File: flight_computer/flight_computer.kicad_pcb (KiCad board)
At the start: 4 copper layers, 89 parts, among them J1 Conn_02x05_Odd_Even, J2 MEM2061-01-188-00-A_REVA, J3 Conn_01x02, J4 Conn_01x07, J5 3817564, Q1 Q_NPN_BEC, Q2 Q_NMOS_GSD, SW1 SW_Push, SW2 SW_Push, U1 STM8S007C8T6TR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

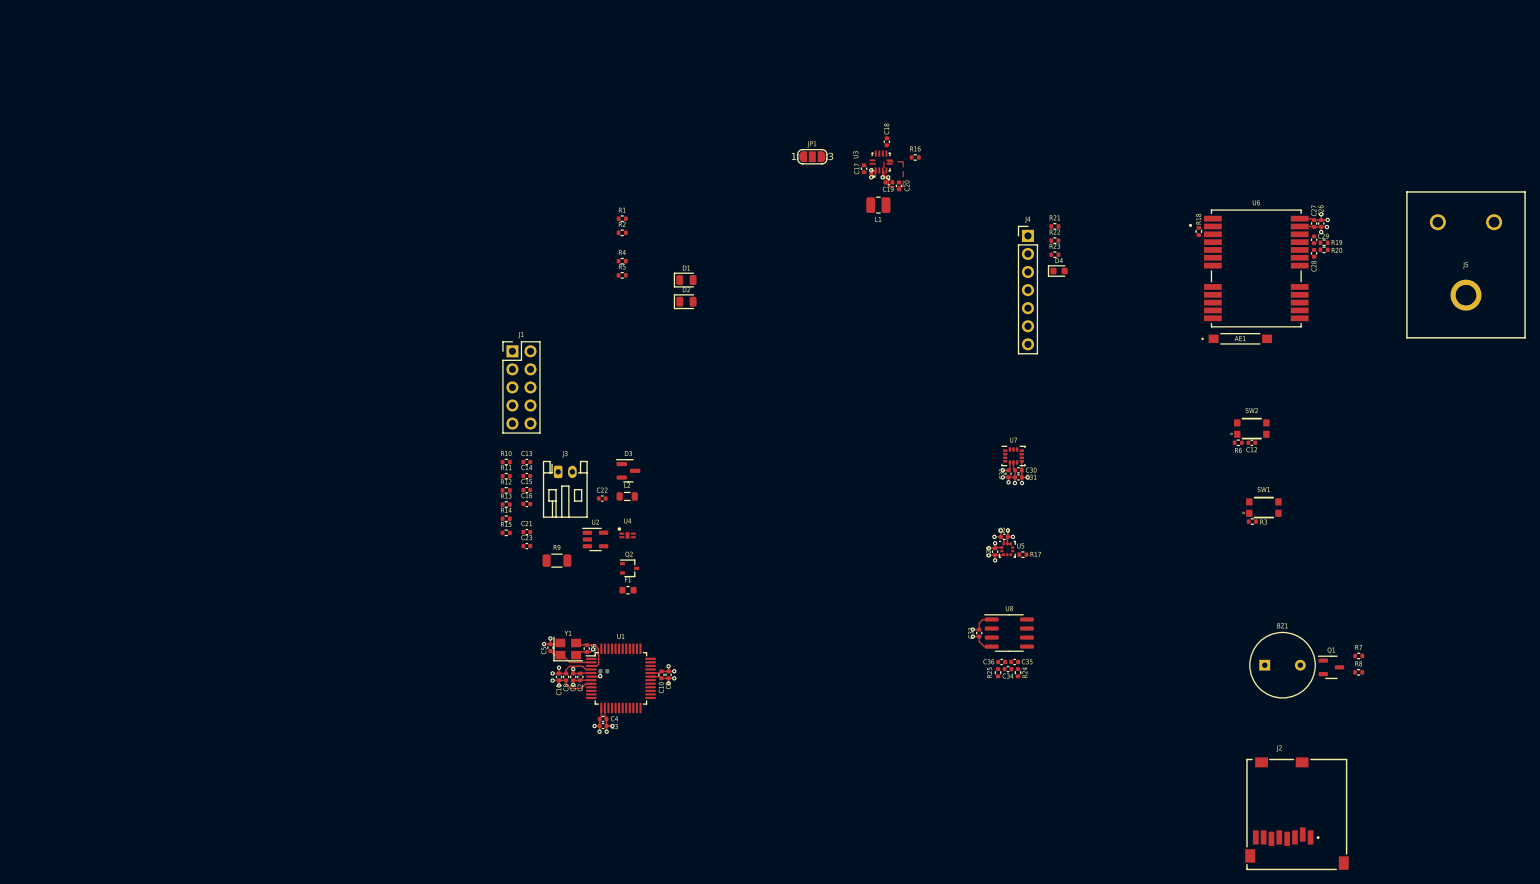
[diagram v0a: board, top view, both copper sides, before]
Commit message: finsihed grouping the layout
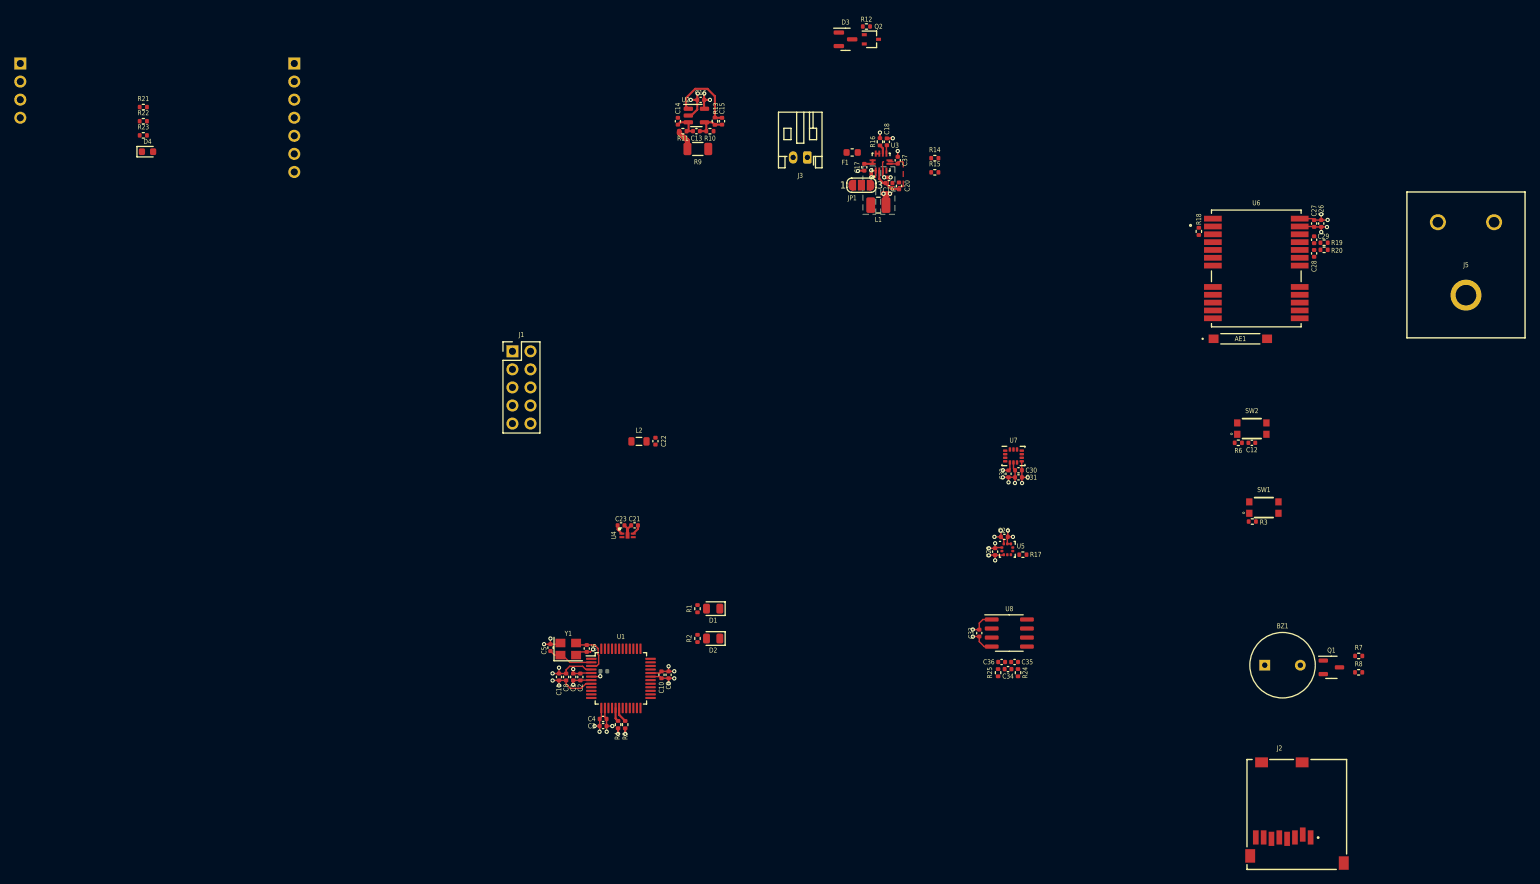
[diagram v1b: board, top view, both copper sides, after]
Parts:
- added C37: 100nF, Capacitor_SMD:C_0402_1005Metric, F.Cu at (190.2, 50.0)
- added J6: Conn_01x04, Connector_PinHeader_2.54mm:PinHeader_1x04_P2.54mm_Vertical, B.Cu at (66.9, 36.4)
- J4: moved to B.Cu
- moved D4 129.2 mm to (84.8, 48.8)
- moved R21 129.2 mm to (84.2, 42.5)
- moved R22 129.2 mm to (84.2, 44.5)
- moved R23 129.2 mm to (84.2, 46.5)
- moved J4 105.9 mm to (105.4, 36.4), turned to 180 degrees
- moved R12 82.5 mm to (185.8, 31.2), turned to 180 degrees
- moved Q2 81.7 mm to (186.5, 33.0)
- moved R15 78.7 mm to (195.4, 51.7)
- moved R14 78.7 mm to (195.4, 49.7)
- moved F1 69.1 mm to (183.8, 48.9)
- moved D3 67.9 mm to (182.9, 33.0)
- moved R4 65.1 mm to (150.9, 129.3), turned to 90 degrees
- moved R5 63.1 mm to (151.9, 129.3), turned to 90 degrees
- moved C16 61.8 mm to (162.5, 41.5), turned to 180 degrees
- moved R13 61.3 mm to (164.5, 44.5), turned to 90 degrees
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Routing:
- net GND: track 44.8 -> 60.5 mm, vias 20 -> 25
- net /Microcontroller/I_{SENSE}: track 0.00 -> 10.7 mm
- net Net-(U2--): track 0.00 -> 4.89 mm
- net /Power/3V3A: track 4.16 -> 8.60 mm, vias 2 -> 4
- net Net-(U2-+): track 0.00 -> 3.77 mm
- net /Microcontroller/3V3D: track 27.4 -> 30.9 mm, vias 11 -> 14
- net /Power/I_{sense_raw}: track 0.00 -> 3.02 mm
- net Net-(U3-L2): track 1.78 -> 4.58 mm, vias 2 -> 4
- net /SCL: track 0.00 -> 2.18 mm
- net /SDA: track 0.00 -> 1.96 mm
- net Net-(JP1-B): track 0.00 -> 1.68 mm
- net /1V8A: track 6.87 -> 8.27 mm
- net /Power/PGOOD: track 0.00 -> 1.32 mm
- net Net-(U3-SS): track 0.00 -> 1.21 mm
- added copper zone on B.Cu, net Net-(U3-L1)
- added copper zone on B.Cu, net Net-(U3-L2)
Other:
- board text added: "E220-400T30D"

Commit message: Layout first effort done
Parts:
- added C38: 100nF, Capacitor_SMD:C_0402_1005Metric, F.Cu at (149.5, 89.8)
- added H1: MountingHole_Pad, MountingHole:MountingHole_3.2mm_M3_Pad_Via, F.Cu at (166.1, 71.5)
- added H2: MountingHole_Pad, MountingHole:MountingHole_3.2mm_M3_Pad_Via, F.Cu at (126.2, 71.5)
- added H3: MountingHole_Pad, MountingHole:MountingHole_3.2mm_M3_Pad_Via, F.Cu at (126.2, 130.5)
- added H4: MountingHole_Pad, MountingHole:MountingHole_3.2mm_M3_Pad_Via, F.Cu at (166.2, 130.5)
- moved J5 125.9 mm to (142.9, 85.1), turned to 180 degrees
- moved J2 121.7 mm to (130.8, 103.6), turned to -90 degrees
- moved C26 116.9 mm to (147.0, 114.7), turned to 180 degrees
- moved C27 116.5 mm to (147.0, 115.7), turned to 180 degrees
- moved J6 115.7 mm to (134.1, 130.7), turned to -90 degrees
- moved R19 113.4 mm to (149.7, 114.3), turned to 90 degrees
- moved C29 113.4 mm to (149.3, 115.7), turned to 180 degrees
- moved R20 112.0 mm to (150.7, 114.3), turned to 90 degrees
- moved R18 110.9 mm to (148.1, 131.9), turned to 0 degrees
- moved C28 110.8 mm to (151.2, 115.7), turned to 0 degrees
- moved U6 105.1 mm to (153.3, 123.9), turned to 90 degrees
- moved R3 102.7 mm to (139.3, 120.8)
- moved SW1 102.7 mm to (140.9, 118.8)
- moved R7 101.3 mm to (156.3, 96.9)
- moved AE1 100.8 mm to (155.7, 132.8), turned to 180 degrees
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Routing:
- net GND: track 60.5 -> 65.4 mm, vias 25 -> 28
- net Net-(JP1-B): track 1.68 -> 5.93 mm
- net /Microcontroller/3V3D: track 30.9 -> 35.1 mm, vias 14 -> 15
- net /RADIO_M0: track 0.00 -> 2.35 mm
- net /RADIO_M1: track 0.00 -> 2.34 mm
- added copper zone on F.Cu, net Net-(JP1-B)
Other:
- board outline added: 47 x 66 mm
- board text added: "BUTTON"
- board text added: "Flight Computer"
- board text added: "RESET"
- board text added: "REV A"
- board text added: "Shaun L. Angus E."

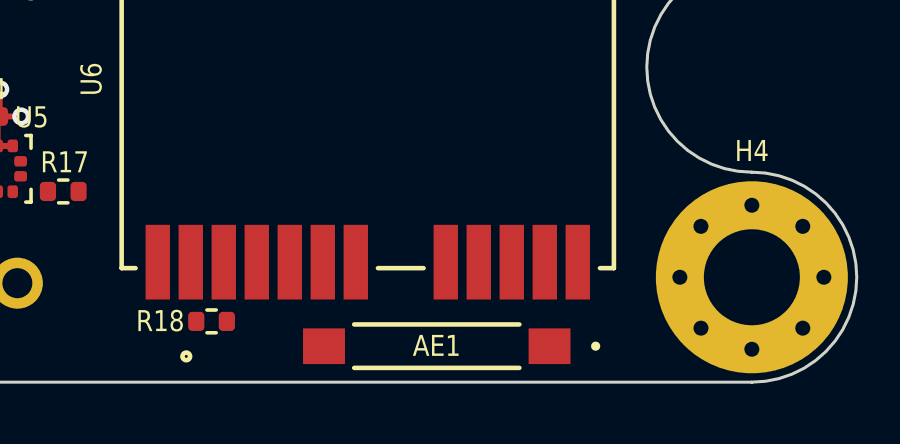
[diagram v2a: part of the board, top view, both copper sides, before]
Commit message: GPS antenna controlled impedance
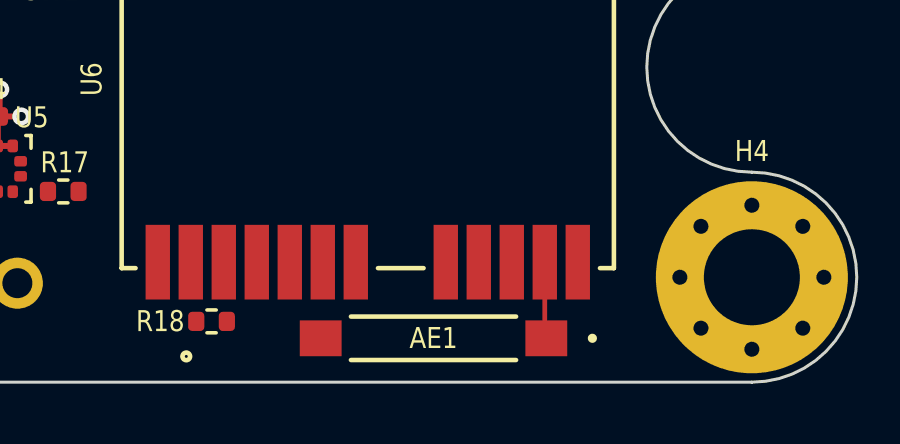
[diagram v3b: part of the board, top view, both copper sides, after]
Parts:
- moved AE1 0.28 mm to (155.5, 132.5)
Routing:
- net Net-(AE1-FEED): track 0.00 -> 2.56 mm
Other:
- board text added: "0.1565 controlled impedance trace width For JLC04161H-3313 4 layer stackup microstrip"
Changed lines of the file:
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@@
   )
   (footprint "my_footprints:ANT_ANT8010LL05R1516A_PUL" (layer "F.Cu")
-    (at 155.65 132.7625 180)
+    (at 155.5408 132.5 180)
     (tags "ANT8010LL05R1516A ")
     (property "Manufacturer PN" "ANT8010LL05R1516A")
@@
       (polygon
         (pts
-          (xy 158.6599 133.3086)
-          (xy 152.6401 133.3086)
-          (xy 152.6401 132.2164)
-          (xy 158.6599 132.2164)
+          (xy 158.5507 133.0461)
+          (xy 152.5309 133.0461)
+          (xy 152.5309 131.9539)
+          (xy 158.5507 131.9539)
         )
       )
@@
     )
   )
-  (gr_rect (start 130.05 133.6625) (end 154.05 90.6625)
+  (gr_rect (start 130.05 90.6625) (end 154.05 133.6625)
     (stroke (width 0.15) (type default)) (fill none) (layer "B.SilkS"))
   (gr_line (start 126.5 113.5) (end 144.1 113.5)
@@
   (gr_rect (start 126.5 111.65) (end 144.1 115.35)
     (stroke (width 0.15) (type default)) (fill none) (layer "F.SilkS"))
+  (gr_circle (center 159.3 131.6) (end 159.8 131.2)
+    (stroke (width 0.15) (type default)) (fill none) (layer "Cmts.User"))
+  (gr_line (start 161.2 138.8) (end 159.3 131.6)
+    (stroke (width 0.15) (type default)) (layer "Cmts.User"))
   (gr_line (start 169.65 116.462502) (end 169.65 85.462498)
     (stroke (width 0.1) (type solid)) (layer "Edge.Cuts"))
@@
     (effects (font (size 1 1) (thickness 0.2) bold) (justify left bottom))
   )
+  (gr_text "0.1565 controlled impedance trace width\nFor JLC04161H-3313 4 layer stackup microstrip" (at 159.6 142.3) (layer "Cmts.User")
+    (effects (font (size 1 1) (thickness 0.15)) (justify left bottom))
+  )
+  (segment (start 159.25 129.9625) (end 159.25 132.45) (width 0.1565) (layer "F.Cu") (net 1))
+  (segment (start 159.25 132.45) (end 159.3 132.5) (width 0.1565) (layer "F.Cu") (net 1))
   (segment (start 147.45 117.7625) (end 147.45 115.7991) (width 0.2) (layer "F.Cu") (net 5))
   (segment (start 149.02 89.8) (end 149.02 88.92) (width 0.2) (layer "F.Cu") (net 5))

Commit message: More PCB layout
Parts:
- added TP1: TestPoint, Connector_PinHeader_2.54mm:PinHeader_1x01_P2.54mm_Vertical, F.Cu at (129.4, 113.2)
- added TP2: TestPoint, Connector_PinHeader_2.54mm:PinHeader_1x01_P2.54mm_Vertical, F.Cu at (124.4, 116.8)
- added TP3: TestPoint, Connector_PinHeader_2.54mm:PinHeader_1x01_P2.54mm_Vertical, F.Cu at (129.4, 116.8)
- added TP4: TestPoint, Connector_PinHeader_2.54mm:PinHeader_1x01_P2.54mm_Vertical, F.Cu at (124.4, 113.2)
- added TP5: TestPoint, Connector_PinHeader_2.54mm:PinHeader_1x01_P2.54mm_Vertical, F.Cu at (131.1, 92.6)
- added TP6: TestPoint, Connector_PinHeader_2.54mm:PinHeader_1x01_P2.54mm_Vertical, F.Cu at (134.4, 113.2)
- added TP7: TestPoint, Connector_PinHeader_2.54mm:PinHeader_1x01_P2.54mm_Vertical, F.Cu at (134.4, 116.8)
- moved C22 20.5 mm to (140.3, 101.6), turned to 180 degrees
- moved L2 16.7 mm to (140.3, 99.3), turned to -90 degrees
- moved D1 9.40 mm to (140.5, 112.5)
- moved R2 9.40 mm to (142.8, 114.7)
- moved D2 9.40 mm to (140.6, 114.7)
- moved R1 9.40 mm to (142.7, 112.5)
- moved C12 1.91 mm to (156.2, 103.4)
- moved SW2 1.91 mm to (156.2, 101.4)
- moved R6 1.91 mm to (154.3, 103.4)
- moved J1 1.86 mm to (167.5, 113.0)
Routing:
- net /Power/3V3A: track 8.60 -> 14.7 mm, vias 4 -> 9
- net /1V8A: track 8.27 -> 13.3 mm, vias 4 -> 0
- net GND: track 65.4 -> 68.4 mm, vias 28 -> 31
- net /Microcontroller/3V3D: track 35.1 -> 37.3 mm, vias 15 -> 17
- added copper zone on In2.Cu, net /Microcontroller/3V3D
- added copper zone on B.Cu, net /Power/3V3A
- added copper zone on In1.Cu, net GND
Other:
- board text added: "MISO"
- board text added: "MOSI"
- board text added: "SCK"
- board text added: "SCL"
- board text added: "SDA"
- board text added: "SD_CS"
- board text added: "TC_CS"

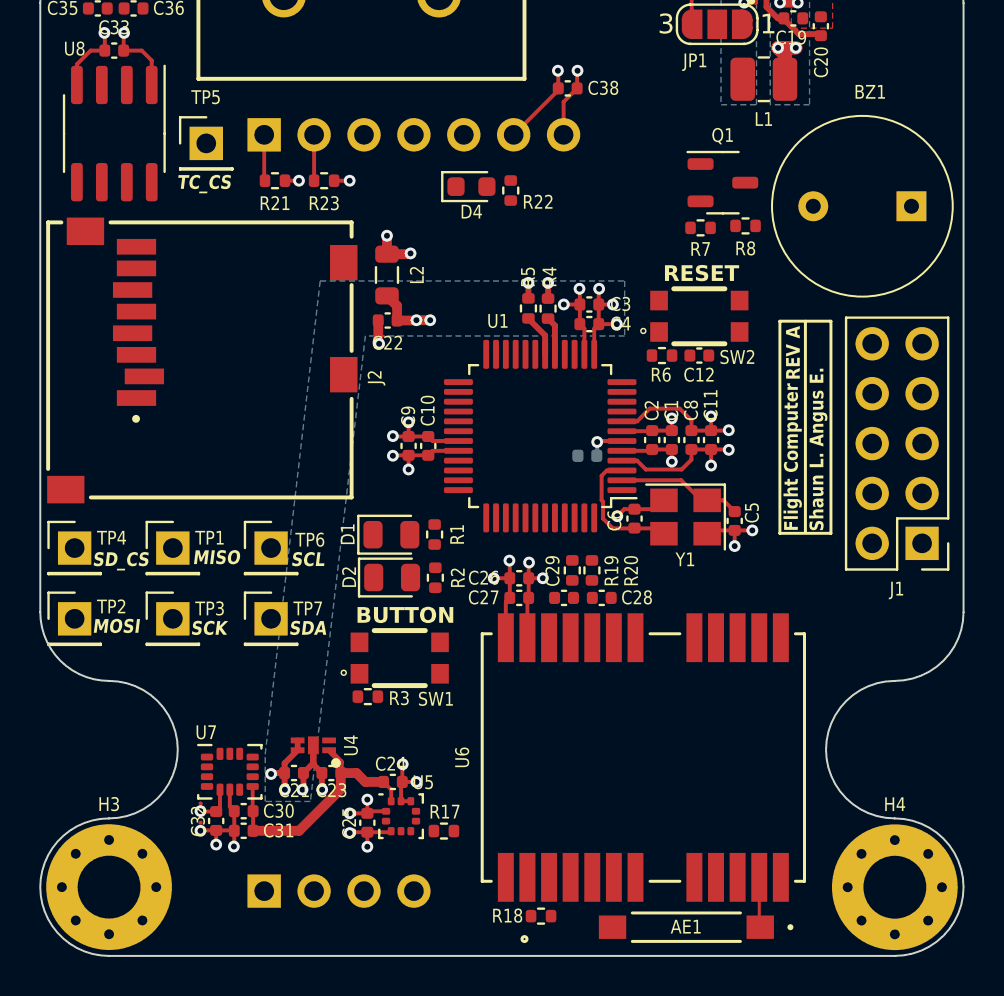
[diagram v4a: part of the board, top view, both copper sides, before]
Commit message: Adding E220-400T30D footprint and 3D model
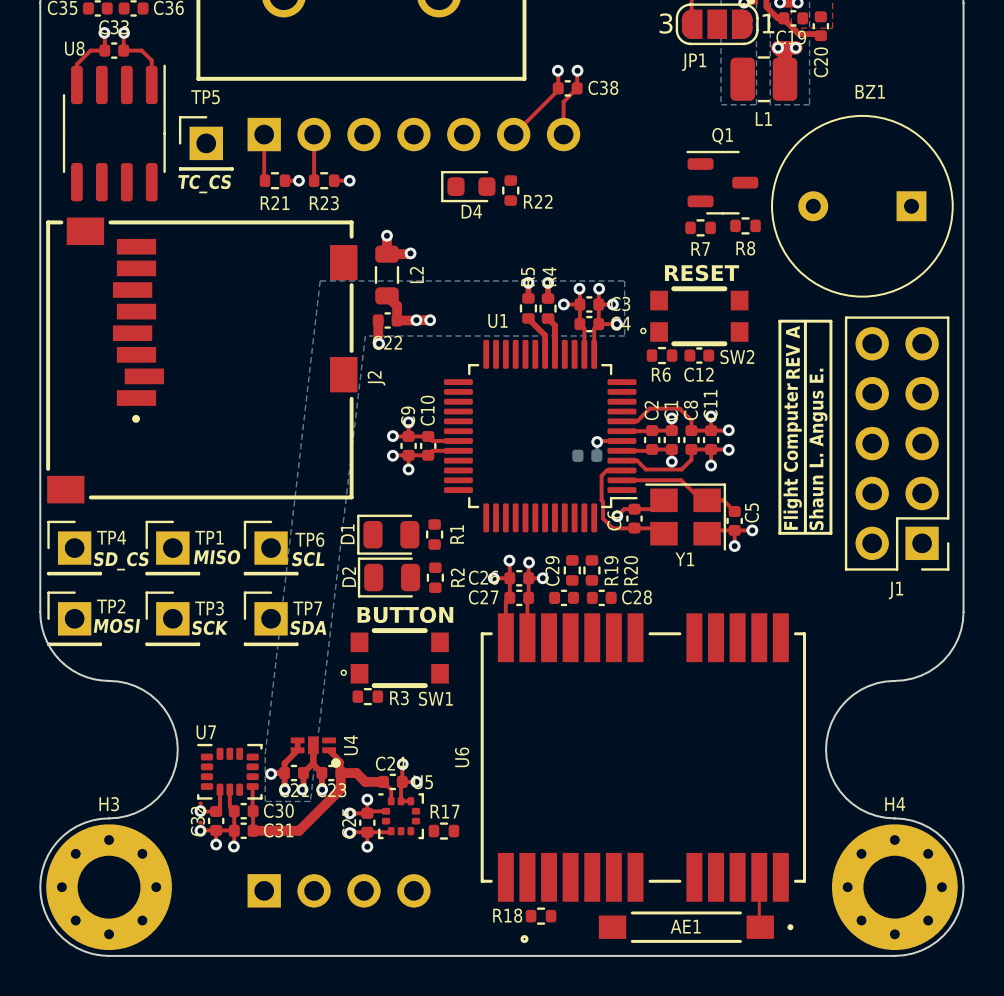
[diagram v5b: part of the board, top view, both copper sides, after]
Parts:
- removed J4: Conn_01x07, Connector_PinHeader_2.54mm:PinHeader_1x07_P2.54mm_Vertical
- removed J6: Conn_01x04, Connector_PinHeader_2.54mm:PinHeader_1x04_P2.54mm_Vertical
- added J7: Conn_01x07_MountingPin, my_footprints:E220-400T30D, B.Cu at (142.8, 111.8)
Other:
- board text removed: "E220-400T30D"
